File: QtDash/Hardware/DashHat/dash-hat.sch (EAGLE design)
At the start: 1 part, among them J1 CONN_20X2

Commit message: - added start of dash hat schematic and board
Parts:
- added C1, C2, C3, C4: 10nF, SparkFun-Capacitors:10NF-0603-50V-10%
- added C5, C7: 0.1uF, SparkFun-Capacitors:0.1UF-0603-25V-5%
- added C6, C8: 1.0uF, SparkFun-Capacitors:1.0UF-0603-16V-10%
- added D1, D2, D3, D4, D5, D6, D7, D8: BAT54, diode:BAT54
- added IC1: LM324, digital_dash:LM324
- added IC2: MCP3X083008, digital_dash:MCP3X083008
- added IC3: MCP23017SP, microchip:MCP23017SP
- added J2, J3, J4, J5: (no value), SparkFun-Connectors:CONN_02
- added OK1, OK2: ILQ1, optocoupler:ILQ1
- added R1, R4, R6, R8: 100, SparkFun-Resistors:100OHM-0603-1/10W-1%
- added R10, R11, R12, R9: 1k, SparkFun-Resistors:1KOHM-0603-1/10W-1%
- added R13, R14, R15, R16: 640k, SparkFun-Resistors:390KOHM-0603-1/10W-1%
- added R2, R3, R5, R7: 330k, SparkFun-Resistors:330KOHM-0603-1/10W-1%
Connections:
- new net 3.3V: C7.1, C8.1, IC2.VDD, IC2.VREF, J1.1, J1.17
- new net 5V: C5.1, C6.1, D1.C, D3.C, D5.C, D7.C, IC1A.V+, J1.2, J1.4, R10.2, R11.2, R12.2, R9.2
- new net ADC1_IN: C1.1, IC2.CH0, R13.2, R2.1
- new net ADC2_IN: C2.1, IC2.CH1, R15.2, R3.1
- new net ADC3_IN: C3.1, IC2.CH2, R14.2, R5.1
- new net ADC4_IN: C4.1, IC2.CH3, R16.2, R7.1
- new net GND: C1.2, C2.2, C3.2, C4.2, C5.2, C6.2, C7.2, C8.2, D2.A, D4.A, D6.A, D8.A, IC1A.V-, IC2.AGND, IC2.DGND, J1.14, J1.20, J1.25, J1.30, J1.39, J1.6, J1.9, J2.1, J3.1, J4.1, J5.1, R13.1, R14.1, R15.1, R16.1
- new net N$1: IC1A.-IN, IC1A.OUT, R2.2
- new net N$11: D5.A, D6.C, IC1C.+IN, R6.2
- new net N$13: IC1D.-IN, IC1D.OUT, R7.2
- new net N$15: D7.A, D8.C, IC1D.+IN, R8.2
- new net N$16: IC2.!CS/SHDN
- new net N$21: IC2.CH4
- new net N$22: IC2.CH5
- new net N$23: IC2.CH6
- new net N$24: IC2.CH7
- new net N$3: D1.A, D2.C, IC1A.+IN, R1.2
- new net N$5: IC1B.-IN, IC1B.OUT, R3.2
- new net N$7: D3.A, D4.C, IC1B.+IN, R4.2
- new net N$9: IC1C.-IN, IC1C.OUT, R5.2
- new net SENSOR1_IN: J2.2, R1.1, R9.1
- new net SENSOR2_IN: J3.2, R10.1, R4.1
- new net SENSOR3_IN: J4.2, R11.1, R6.1
- new net SENSOR4_IN: J5.2, R12.1, R8.1
- new net SPI_CE0_N: J1.24
- new net SPI_CE1_N: J1.26
- new net SPI_CLK: IC2.CLK, J1.23
- new net SPI_MISO: IC2.DOUT, J1.21
- new net SPI_MOSI: IC2.DIN, J1.19
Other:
- moved on the sheet: J1

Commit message: digital-dash-project: 	- added start of circular connector 31 	- added pos/neg isolated inputs and hooked up gpio expander 	- todo: get measurements on connector 32 and connector 31 to be able to finish schematic
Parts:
- added C10: 1.0uF, SparkFun-Capacitors:1.0UF-0603-16V-10%
- added C9: 0.1uF, SparkFun-Capacitors:0.1UF-0603-25V-5%
- added OK3: ILQ1, optocoupler:ILQ1
- added R17, R18, R19, R20, R21, R22, R23, R24, R25, R26, R27, R28, R29, R30, R31, R32, R33, R34, R35, R36, R37, R38, R39, R40, R41, R42, R43, R44, R45, R46, R47, R48, R49, R50, R51, R52: 470, SparkFun-Resistors:470OHM-0603-1/10W-1%
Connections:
- new net 12V: R17.2, R20.2, R23.2, R25.2, R29.2, R32.2, R35.2, R37.2, R41.2, R44.2, R47.2, R49.2
- new net 5V1: C10.1, C9.1
- new net IN10N: OK3B.C, R45.2
- new net IN10P: OK3B.A, R44.1
- new net IN11N: OK3C.C, R48.2
- new net IN11P: OK3C.A, R47.1
- new net IN12N: OK3D.C, R50.2
- new net IN12P: OK3D.A, R49.1
- new net IN1N: OK1A.C, R18.2
- new net IN1P: OK1A.A, R17.1
- new net IN2N: OK1B.C, R21.2
- new net IN2P: OK1B.A, R20.1
- new net IN3N: OK1C.C, R24.2
- new net IN3P: OK1C.A, R23.1
- new net IN4N: OK1D.C, R26.2
- new net IN4P: OK1D.A, R25.1
- new net IN5N: OK2A.C, R30.2
- new net IN5P: OK2A.A, R29.1
- new net IN6N: OK2B.C, R33.2
- new net IN6P: OK2B.A, R32.1
- new net IN7N: OK2C.C, R36.2
- new net IN7P: OK2C.A, R35.1
- new net IN8N: OK2D.C, R38.2
- new net IN8P: OK2D.A, R37.1
- new net IN9N: OK3A.C, R42.2
- new net IN9P: OK3A.A, R41.1
- new net N$10: IC3.GPB4
- new net N$12: IC3.GPB5
- new net N$14: IC3.GPB6
- new net N$17: IC3.GPB7
- new net OUT1: IC3.GPA0, OK1A.COL, R19.1
- new net OUT10: IC3.GPB1, OK3B.COL, R46.1
- new net OUT11: IC3.GPB2, OK3C.COL, R51.1
- new net OUT12: IC3.GPB3, OK3D.COL, R52.1
- new net OUT2: IC3.GPA1, OK1B.COL, R22.1
- new net OUT3: IC3.GPA2, OK1C.COL, R27.1
- new net OUT4: IC3.GPA3, OK1D.COL, R28.1
- new net OUT5: IC3.GPA4, OK2A.COL, R31.1
- new net OUT6: IC3.GPA5, OK2B.COL, R34.1
- new net OUT7: IC3.GPA6, OK2C.COL, R39.1
- new net OUT8: IC3.GPA7, OK2D.COL, R40.1
- new net OUT9: IC3.GPB0, OK3A.COL, R43.1
- new net SCL: IC3.SCL, J1.5
- new net SDA: IC3.SDA, J1.3
- net 3.3V: now also IC3.!RESET, IC3.VDD, R18.1, R19.2, R21.1, R22.2, R24.1, R26.1, R27.2, R28.2, R30.1, R31.2, R33.1, R34.2, R36.1, R38.1, R39.2, R40.2, R42.1, R43.2, R45.1, R46.2, R48.1, R50.1, R51.2, R52.2
- net GND: now also C10.2, C9.2, IC3.A0, IC3.A1, IC3.A2, IC3.VSS, OK1A.EMIT, OK1B.EMIT, OK2A.EMIT, OK2B.EMIT, OK2C.EMIT, OK2D.EMIT, OK3A.EMIT, OK3B.EMIT, OK3C.EMIT, OK3D.EMIT
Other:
- moved on the sheet: IC3, OK1A, OK1B, OK1C, OK1D, OK2A, OK2B, OK2C, OK2D

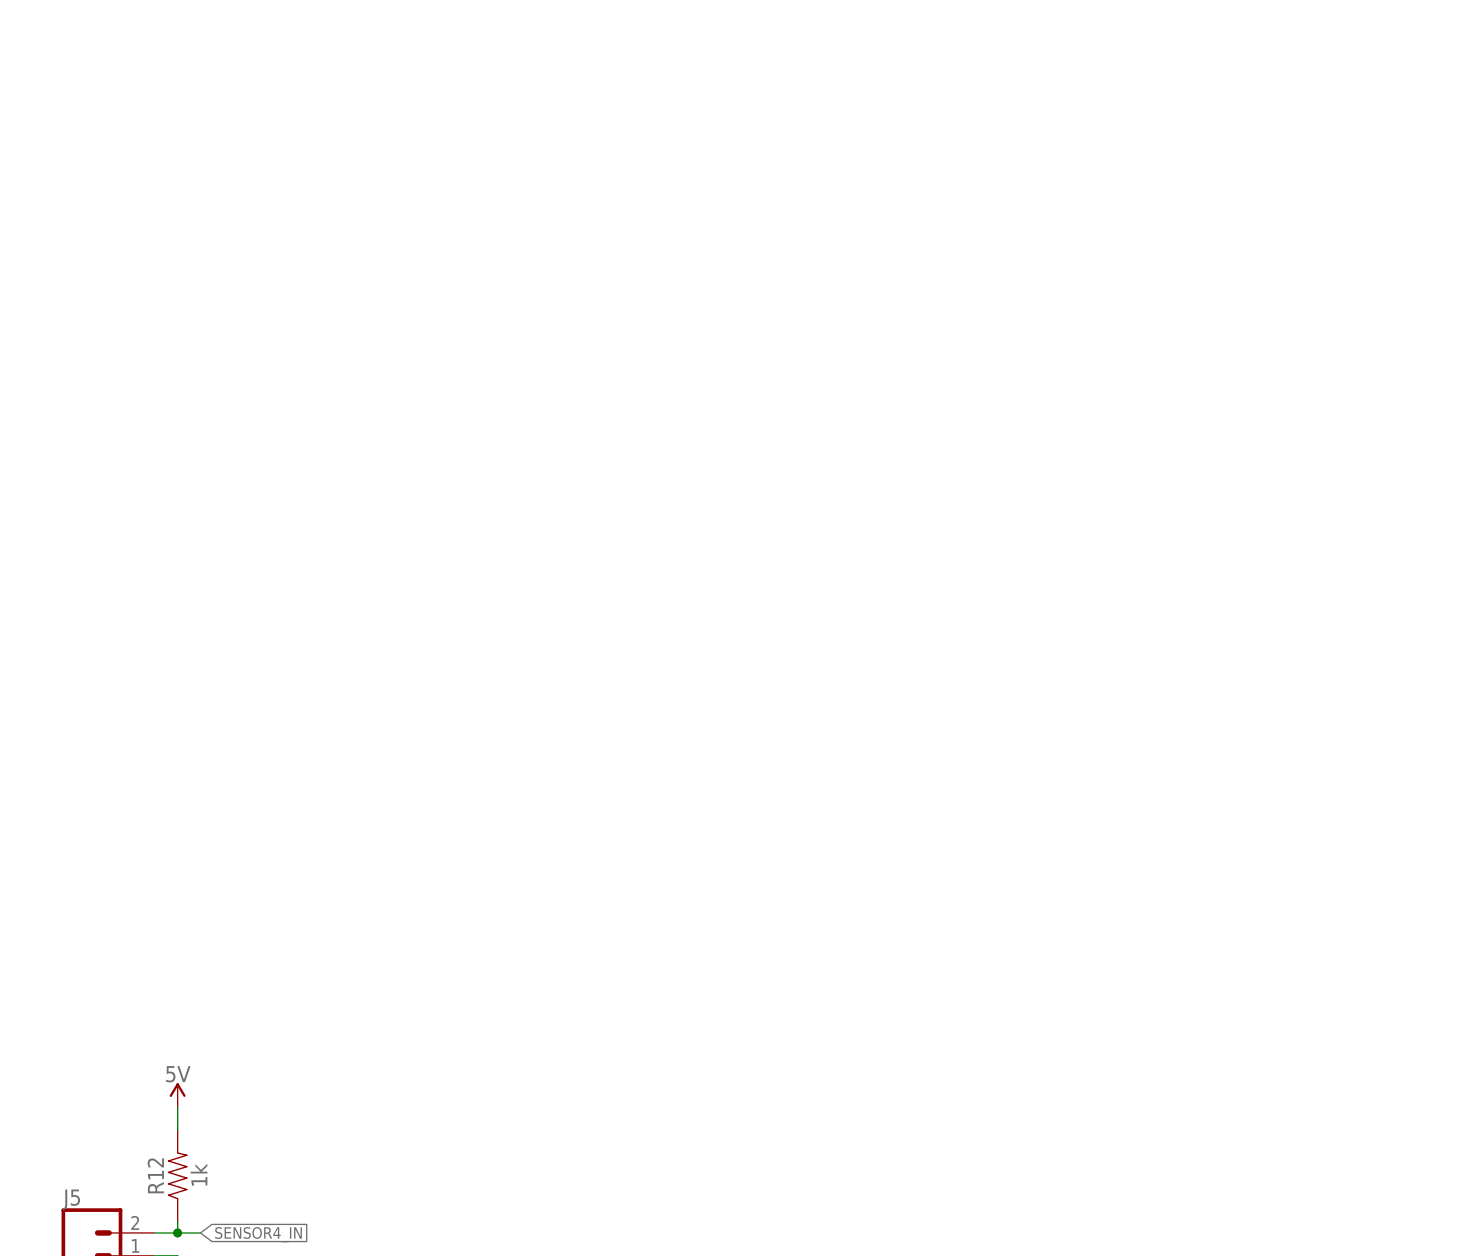
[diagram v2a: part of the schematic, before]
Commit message: - added IL300 to library -- need to have isolated 0-12V input to 0-3.3V output 	- added start of non-isolated 0-12V input -- need to change to use IL300 ($$$) x2 at least.
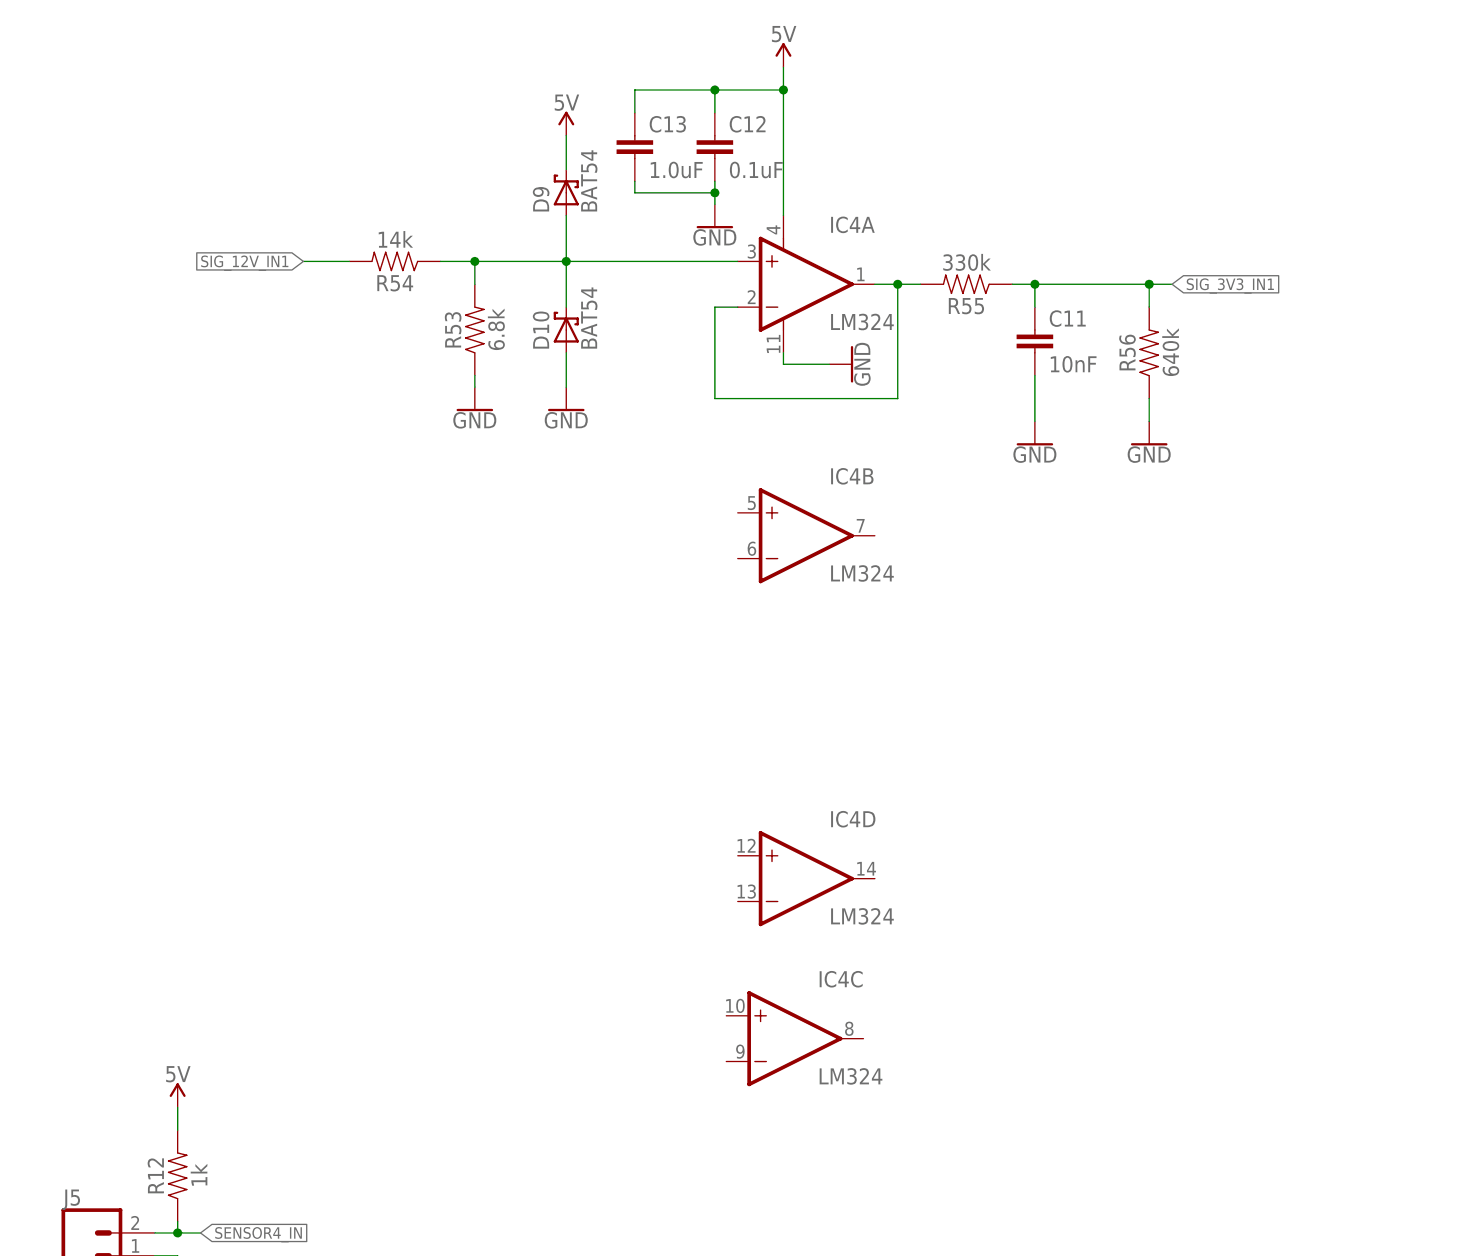
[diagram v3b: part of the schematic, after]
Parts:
- added C11: 10nF, SparkFun-Capacitors:10NF-0603-50V-10%
- added C12: 0.1uF, SparkFun-Capacitors:0.1UF-0603-25V-5%
- added C13: 1.0uF, SparkFun-Capacitors:1.0UF-0603-16V-10%
- added D10, D9: BAT54, diode:BAT54
- added IC4: LM324, digital_dash:LM324
- added R53: 6.8k, SparkFun-Resistors:6.8KOHM-0603-1/10W-1%
- added R54: 14k, SparkFun-Resistors:14KOHM-0603-1/10W-1%
- added R55: 330k, SparkFun-Resistors:330KOHM-0603-1/10W-1%
- added R56: 640k, SparkFun-Resistors:390KOHM-0603-1/10W-1%
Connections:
- new net N$2: D10.C, D9.A, IC4A.+IN, R53.2, R54.1
- new net N$4: IC4A.-IN, IC4A.OUT, R55.2
- new net SIG_12V_IN1: R54.2
- new net SIG_3V3_IN1: C11.1, R55.1, R56.2
- net 5V: now also C12.1, C13.1, D9.C, IC4A.V+
- net GND: now also C11.2, C12.2, C13.2, D10.A, IC4A.V-, R53.1, R56.1
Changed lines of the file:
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@@
 <part name="SUPPLY37" library="SparkFun-PowerSymbols" deviceset="3.3V" device=""/>
 <part name="GND48" library="SparkFun-PowerSymbols" deviceset="GND" device=""/>
+<part name="IC4" library="digital_dash" deviceset="LM324" device=""/>
+<part name="D9" library="diode" deviceset="BAT54" device=""/>
+<part name="D10" library="diode" deviceset="BAT54" device=""/>
+<part name="R53" library="SparkFun-Resistors" deviceset="6.8KOHM" device="-0603-1/10W-1%" value="6.8k"/>
+<part name="R54" library="SparkFun-Resistors" deviceset="14KOHM" device="-0603-1/10W-1%" value="14k"/>
+<part name="GND49" library="SparkFun-PowerSymbols" deviceset="GND" device=""/>
+<part name="GND50" library="SparkFun-PowerSymbols" deviceset="GND" device=""/>
+<part name="SUPPLY38" library="SparkFun-PowerSymbols" deviceset="5V" device=""/>
+<part name="R55" library="SparkFun-Resistors" deviceset="330KOHM" device="-0603-1/10W-1%" value="330k"/>
+<part name="R56" library="SparkFun-Resistors" deviceset="390KOHM" device="-0603-1/10W-1%" value="640k"/>
+<part name="C11" library="SparkFun-Capacitors" deviceset="10NF" device="-0603-50V-10%" value="10nF"/>
+<part name="GND51" library="SparkFun-PowerSymbols" deviceset="GND" device=""/>
+<part name="GND52" library="SparkFun-PowerSymbols" deviceset="GND" device=""/>
+<part name="SUPPLY39" library="SparkFun-PowerSymbols" deviceset="5V" device=""/>
+<part name="C12" library="SparkFun-Capacitors" deviceset="0.1UF" device="-0603-25V-5%" value="0.1uF"/>
+<part name="GND53" library="SparkFun-PowerSymbols" deviceset="GND" device=""/>
+<part name="C13" library="SparkFun-Capacitors" deviceset="1.0UF" device="-0603-16V-10%" value="1.0uF"/>
+<part name="GND54" library="SparkFun-PowerSymbols" deviceset="GND" device=""/>
 </parts>
 <sheets>
@@
 <instance part="SUPPLY37" gate="G$1" x="429.26" y="-25.4"/>
 <instance part="GND48" gate="1" x="429.26" y="-58.42"/>
+<instance part="IC4" gate="A" x="287.02" y="279.4"/>
+<instance part="IC4" gate="B" x="287.02" y="251.46"/>
+<instance part="IC4" gate="C" x="285.75" y="195.58"/>
+<instance part="IC4" gate="D" x="287.02" y="213.36"/>
+<instance part="D9" gate="G$1" x="260.35" y="289.56" rot="R90"/>
+<instance part="D10" gate="G$1" x="260.35" y="274.32" rot="R90"/>
+<instance part="R53" gate="G$1" x="250.19" y="274.32" rot="R90"/>
+<instance part="R54" gate="G$1" x="241.3" y="281.94" rot="R180"/>
+<instance part="GND49" gate="1" x="250.19" y="265.43"/>
+<instance part="GND50" gate="1" x="260.35" y="265.43"/>
+<instance part="SUPPLY38" gate="G$1" x="260.35" y="295.91"/>
+<instance part="R55" gate="G$1" x="304.8" y="279.4" rot="R180"/>
+<instance part="R56" gate="G$1" x="325.12" y="271.78" rot="R90"/>
+<instance part="C11" gate="G$1" x="312.42" y="271.78"/>
+<instance part="GND51" gate="1" x="312.42" y="261.62"/>
+<instance part="GND52" gate="1" x="325.12" y="261.62"/>
+<instance part="SUPPLY39" gate="G$1" x="284.48" y="303.53"/>
+<instance part="C12" gate="G$1" x="276.86" y="293.37"/>
+<instance part="GND53" gate="1" x="276.86" y="285.75"/>
+<instance part="C13" gate="G$1" x="267.97" y="293.37"/>
+<instance part="GND54" gate="1" x="292.1" y="270.51" rot="R90"/>
 </instances>
 <busses>
@@
 <pinref part="OK3" gate="D" pin="EMIT"/>
 </segment>
+<segment>
+<pinref part="GND49" gate="1" pin="GND"/>
+<pinref part="R53" gate="G$1" pin="1"/>
+<wire x1="250.19" y1="267.97" x2="250.19" y2="269.24" width="0.1524" layer="91"/>
+</segment>
+<segment>
+<pinref part="D10" gate="G$1" pin="A"/>
+<wire x1="260.35" y1="271.78" x2="260.35" y2="267.97" width="0.1524" layer="91"/>
+<pinref part="GND50" gate="1" pin="GND"/>
+</segment>
+<segment>
+<pinref part="C11" gate="G$1" pin="2"/>
+<wire x1="312.42" y1="269.24" x2="312.42" y2="264.16" width="0.1524" layer="91"/>
+<pinref part="GND51" gate="1" pin="GND"/>
+</segment>
+<segment>
+<pinref part="R56" gate="G$1" pin="1"/>
+<wire x1="325.12" y1="266.7" x2="325.12" y2="264.16" width="0.1524" layer="91"/>
+<pinref part="GND52" gate="1" pin="GND"/>
+</segment>
+<segment>
+<pinref part="C12" gate="G$1" pin="2"/>
+<pinref part="GND53" gate="1" pin="GND"/>
+<wire x1="276.86" y1="290.83" x2="276.86" y2="289.56" width="0.1524" layer="91"/>
+<pinref part="C13" gate="G$1" pin="2"/>
+<wire x1="276.86" y1="289.56" x2="276.86" y2="288.29" width="0.1524" layer="91"/>
+<wire x1="276.86" y1="289.56" x2="267.97" y2="289.56" width="0.1524" layer="91"/>
+<wire x1="267.97" y1="289.56" x2="267.97" y2="290.83" width="0.1524" layer="91"/>
+<junction x="276.86" y="289.56"/>
+</segment>
+<segment>
+<pinref part="GND54" gate="1" pin="GND"/>
+<pinref part="IC4" gate="A" pin="V-"/>
+<wire x1="289.56" y1="270.51" x2="284.48" y2="270.51" width="0.1524" layer="91"/>
+<wire x1="284.48" y1="270.51" x2="284.48" y2="271.78" width="0.1524" layer="91"/>
+</segment>
 </net>
 <net name="5V" class="0">
@@
 <wire x1="39.37" y1="73.66" x2="48.26" y2="73.66" width="0.1524" layer="91"/>
 <junction x="48.26" y="73.66"/>
+</segment>
+<segment>
+<pinref part="D9" gate="G$1" pin="C"/>
+<wire x1="260.35" y1="292.1" x2="260.35" y2="295.91" width="0.1524" layer="91"/>
+<pinref part="SUPPLY38" gate="G$1" pin="5V"/>
+</segment>
+<segment>
+<pinref part="SUPPLY39" gate="G$1" pin="5V"/>
+<wire x1="284.48" y1="287.02" x2="284.48" y2="300.99" width="0.1524" layer="91"/>
+<pinref part="C12" gate="G$1" pin="1"/>
+<wire x1="284.48" y1="300.99" x2="284.48" y2="303.53" width="0.1524" layer="91"/>
+<wire x1="276.86" y1="298.45" x2="276.86" y2="300.99" width="0.1524" layer="91"/>
+<wire x1="276.86" y1="300.99" x2="284.48" y2="300.99" width="0.1524" layer="91"/>
+<junction x="284.48" y="300.99"/>
+<pinref part="C13" gate="G$1" pin="1"/>
+<wire x1="276.86" y1="300.99" x2="267.97" y2="300.99" width="0.1524" layer="91"/>
+<wire x1="267.97" y1="300.99" x2="267.97" y2="298.45" width="0.1524" layer="91"/>
+<junction x="276.86" y="300.99"/>
+<pinref part="IC4" gate="A" pin="V+"/>
 </segment>
 </net>
@@
 </segment>
 </net>
+<net name="N$2" class="0">
+<segment>
+<pinref part="R53" gate="G$1" pin="2"/>
+<pinref part="R54" gate="G$1" pin="1"/>
+<wire x1="250.19" y1="279.4" x2="250.19" y2="281.94" width="0.1524" layer="91"/>
+<pinref part="D9" gate="G$1" pin="A"/>
+<pinref part="D10" gate="G$1" pin="C"/>
+<wire x1="250.19" y1="281.94" x2="246.38" y2="281.94" width="0.1524" layer="91"/>
+<wire x1="260.35" y1="287.02" x2="260.35" y2="281.94" width="0.1524" layer="91"/>
+<wire x1="260.35" y1="281.94" x2="260.35" y2="276.86" width="0.1524" layer="91"/>
+<wire x1="250.19" y1="281.94" x2="260.35" y2="281.94" width="0.1524" layer="91"/>
+<junction x="250.19" y="281.94"/>
+<junction x="260.35" y="281.94"/>
+<pinref part="IC4" gate="A" pin="+IN"/>
+<wire x1="260.35" y1="281.94" x2="279.4" y2="281.94" width="0.1524" layer="91"/>
+</segment>
+</net>
+<net name="SIG_12V_IN1" class="0">
+<segment>
+<pinref part="R54" gate="G$1" pin="2"/>
+<wire x1="236.22" y1="281.94" x2="231.14" y2="281.94" width="0.1524" layer="91"/>
+<label x="231.14" y="281.94" size="1.27" layer="95" rot="R180" xref="yes"/>
+</segment>
+</net>
+<net name="N$4" class="0">
+<segment>
+<pinref part="IC4" gate="A" pin="OUT"/>
+<pinref part="R55" gate="G$1" pin="2"/>
+<wire x1="299.72" y1="279.4" x2="297.18" y2="279.4" width="0.1524" layer="91"/>
+<pinref part="IC4" gate="A" pin="-IN"/>
+<wire x1="297.18" y1="279.4" x2="294.64" y2="279.4" width="0.1524" layer="91"/>
+<wire x1="279.4" y1="276.86" x2="276.86" y2="276.86" width="0.1524" layer="91"/>
+<wire x1="276.86" y1="276.86" x2="276.86" y2="266.7" width="0.1524" layer="91"/>
+<wire x1="276.86" y1="266.7" x2="297.18" y2="266.7" width="0.1524" layer="91"/>
+<wire x1="297.18" y1="266.7" x2="297.18" y2="279.4" width="0.1524" layer="91"/>
+<junction x="297.18" y="279.4"/>
+</segment>
+</net>
+<net name="SIG_3V3_IN1" class="0">
+<segment>
+<pinref part="R55" gate="G$1" pin="1"/>
+<pinref part="C11" gate="G$1" pin="1"/>
+<wire x1="309.88" y1="279.4" x2="312.42" y2="279.4" width="0.1524" layer="91"/>
+<wire x1="312.42" y1="279.4" x2="312.42" y2="276.86" width="0.1524" layer="91"/>
+<pinref part="R56" gate="G$1" pin="2"/>
+<wire x1="312.42" y1="279.4" x2="325.12" y2="279.4" width="0.1524" layer="91"/>
+<wire x1="325.12" y1="279.4" x2="325.12" y2="276.86" width="0.1524" layer="91"/>
+<junction x="312.42" y="279.4"/>
+<wire x1="325.12" y1="279.4" x2="327.66" y2="279.4" width="0.1524" layer="91"/>
+<junction x="325.12" y="279.4"/>
+<label x="327.66" y="279.4" size="1.27" layer="95" xref="yes"/>
+</segment>
+</net>
